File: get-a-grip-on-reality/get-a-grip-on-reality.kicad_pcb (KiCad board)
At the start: 2 copper layers, 74 parts, among them J1 HALL1, J10 MOTOR4, J11 MOTOR5, J12 Conn_01x04_Pin, J13 Conn_01x05_Pin, J14 Battery Connector Bat, J15 Battery Connector MCU, J2 HALL2, J3 HALL3, J4 HALL4, J5 HALL5, J6 Conn_01x04_Pin, J7 MOTOR1, J8 MOTOR2, J9 MOTOR3, P1 USB_C_Plug_USB2.0, U1 TLV76733DRVx, U2 ESP32-S3-WROOM-1, U3 D3V3XA4B10LP, U4 IIM-42652, U5 BQ25887, U6 TPS54KB20RZRR

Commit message: finish top pcb
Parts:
- removed the J12 at (47.1, 44.5)
- added C12: 5p, Capacitor_SMD:C_0805_2012Metric, F.Cu at (81.0, 54.6)
- added C13: 10n, Capacitor_SMD:C_0805_2012Metric, F.Cu at (73.2, 52.8)
- added D4: BPV22NF, BPV22NF:XDCR_BPV22NF, F.Cu at (80.3, 49.0)
- added D5: BPV22NF, BPV22NF:XDCR_BPV22NF, F.Cu at (86.1, 52.4)
- added D6: BPV22NF, BPV22NF:XDCR_BPV22NF, F.Cu at (86.1, 45.7)
- added J13: Conn_01x05_Pin, Connector_PinHeader_2.54mm:PinHeader_1x05_P2.54mm_Vertical, F.Cu at (46.9, 45.0)
- added R12: 5.23k, Resistor_SMD:R_0805_2012Metric, F.Cu at (47.9, 150.0)
- added R13: 30.1k, Resistor_SMD:R_0805_2012Metric, F.Cu at (45.9, 150.0)
- added R4: 3k, Resistor_SMD:R_0805_2012Metric, F.Cu at (68.6, 45.3)
- added R5: 47k, Resistor_SMD:R_0805_2012Metric, F.Cu at (68.6, 48.8)
- added R6: 100k, Resistor_SMD:R_0805_2012Metric, F.Cu at (80.9, 52.6)
- added R7: 47k, Resistor_SMD:R_0805_2012Metric, F.Cu at (72.6, 44.4)
- added TH1: 10k, Resistor_SMD:R_0805_2012Metric, F.Cu at (44.0, 150.0)
- added U5: TLV2462CDR, fydp:SOIC127P599X175-8N, F.Cu at (73.3, 49.0)
- P1, U3: moved to B.Cu
- moved P1 34.1 mm to (62.2, 75.4), turned to 180 degrees
- moved C11 28.7 mm to (58.0, 43.8)
- moved U3 23.6 mm to (63.0, 69.3), turned to -90 degrees
- moved D3 11.7 mm to (78.2, 58.1), turned to -90 degrees
- moved R2 7.35 mm to (66.5, 48.8), turned to 90 degrees
- moved R3 6.86 mm to (78.3, 54.6), turned to 90 degrees
- moved C1 4.16 mm to (73.2, 63.5)
- moved J12 4.15 mm to (76.6, 66.8)
- moved C3 3.33 mm to (72.6, 42.2)
- moved C2 3.33 mm to (79.5, 42.2)
- moved R1 3.33 mm to (76.0, 42.2)
- moved U1 3.17 mm to (73.3, 61.1)
- moved D2 2.44 mm to (66.5, 52.4), turned to -90 degrees
- moved C4 1.96 mm to (72.9, 57.8)
- moved C5 1.96 mm to (72.9, 55.7)
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- renumbered C12 to C14, C13 to C15, C14 to C16, C15 to C17, C16 to C18, C17 to C19, C18 to C20, C19 to C21, C20 to C22, C21 to C23, C22 to C24, C23 to C25, C24 to C26, C25 to C27, C26 to C28, C27 to C29, C28 to C30, D4 to D7, D5 to D8, J6 to J1, J15 to J12, J13 to J14, J14 to J15, J1 to J2, J2 to J3, J3 to J4, J4 to J5, J5 to J6, R6 to R10, R7 to R11, R8 to R14, R9 to R15, R10 to R16, R11 to R17, R12 to R18, R13 to R19, R14 to R20, R4 to R8, R5 to R9, U5 to U6, U6 to U7
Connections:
- P1 pad A4: VBUS -> +5V
- P1 pad A9: VBUS -> +5V
- P1 pad B4: VBUS -> +5V
- P1 pad B9: VBUS -> +5V
- U2 pad 16: unconnected-(U2-GPIO46_HALL4B-Pad16) -> Net-(J13-Pin_4)
- U2 pad 22: unconnected-(U2-GPIO14/TOUCH14/ADC2_CH3/FSPIWP/FSPIDQS/SUBSPIWP-Pad22) -> /Light Sensor/2OUT
- U3 pad 4: VBUS -> +5V
- U3 pad 7: VBUS -> +5V
- U6 pad 7: unconnected-(U5-TS-Pad7) -> Net-(U6-TS)
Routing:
- net +3.3V: track 0.00 -> 118.9 mm, vias 0 -> 2
- net Net-(U2-EN): track 0.00 -> 99.8 mm, vias 0 -> 2
- net +5V: track 0.00 -> 24.5 mm, vias 0 -> 3
- net /Light Sensor/1IN-: track 0.00 -> 22.3 mm
- net /MCU/USB_N: track 25.4 -> 7.63 mm, vias 0 -> 1
- net Net-(J13-Pin_3): track 0.00 -> 16.8 mm, vias 0 -> 1
- net /MCU/USB_P: track 22.8 -> 6.54 mm, vias 0 -> 1
- net /Light Sensor/2OUT: track 0.00 -> 12.8 mm
- net Net-(J13-Pin_2): track 0.00 -> 11.5 mm, vias 0 -> 1
- net /HALL4C: track 0.00 -> 10.8 mm
- net /Light Sensor/2IN+: track 0.00 -> 9.88 mm
- net /HALL4B: track 0.00 -> 9.45 mm
- net Net-(U5-1OUT): track 0.00 -> 9.36 mm
- net /HALL4A: track 0.00 -> 7.52 mm
- net /HALL5C: track 0.00 -> 4.41 mm
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- added copper zone on B.Cu, net +5V
- added copper zone on B.Cu, net GND
- added copper zone on F.Cu, net GND
- removed copper zone on F.Cu, net +BATT
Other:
- board text added: "I2C"
- board text added: "M1"
- board text added: "M2"
- board text added: "M3"
- board text added: "M4"
- board text added: "M5"

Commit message: added review comments
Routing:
- net +3.3V: track 118.9 -> 117.3 mm
- net /MCU/USB_N: track 7.63 -> 6.35 mm
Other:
- board text added: "<- Fix long 3.3v line with thin width"
- board text added: "<- GND not connected"
- board text added: "<- More vias here to reduce GND return path impedence"
- board text added: "<- Try not to put vias on pads"
- board text added: "<- add vias here"
- board text added: "Cap here ->"
- board text added: "Missing connection ->"
- board text added: "Move caps ["
- board text added: "Really thin GND path ->"
- board text added: "Rotate cap to reduce return loop V"
- board text added: "^ Right Angle grrr"

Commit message: add pdb
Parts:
- C14, C15, C16, C17, C18, C19, C20, C21, C22, C23, C24, C25, C26, C27, C28, C29, C30, D7, J14, L1, L2, R10, R11, R12, R13, R14, R15, R16, R17, R18, R19, R20, R8, R9, TH1, U6, U7: moved to B.Cu
- moved J14 54.1 mm to (88.7, 117.8), turned to 180 degrees
- moved C14 50.0 mm to (85.6, 107.8)
- moved R9 48.7 mm to (85.8, 125.1)
- moved D7 48.4 mm to (85.6, 111.5)
- moved R8 48.4 mm to (85.6, 114.9)
- moved TH1 45.2 mm to (83.8, 128.6)
- moved R17 45.2 mm to (83.8, 125.1)
- moved R13 41.7 mm to (81.8, 128.6)
- moved R18 41.7 mm to (81.8, 125.1)
- moved U6 41.2 mm to (81.5, 119.5), turned to 180 degrees
- moved L1 40.0 mm to (80.8, 113.4), turned to 180 degrees
- moved C21 39.4 mm to (80.4, 115.7), turned to 0 degrees
- moved R12 38.4 mm to (79.8, 128.6)
- moved C24 38.3 mm to (79.8, 125.1)
- moved C15 35.1 mm to (77.8, 123.5)
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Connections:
- C14 pad 1: VBUS -> +5V
- J15 pad 1: +5V -> GND
- J15 pad 2: GND -> +5V
- U6 pad 23: VBUS -> +5V
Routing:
- net /Power/CELL_1: track 0.00 -> 65.5 mm, vias 0 -> 30
- net +5V: track 24.5 -> 80.5 mm, vias 3 -> 5
- net Net-(U6-TS): track 2.74 -> 14.0 mm, vias 0 -> 2
- net Net-(U7-VCC): track 0.00 -> 10.4 mm, vias 0 -> 1
- net Net-(U7-MSEL): track 2.52 -> 6.11 mm
- net GND: track 4.32 -> 7.28 mm
- net +BATT: vias 0 -> 37
- added copper zone on B.Cu, net +BATT
- added copper zone on F.Cu, net +BATT
- added copper zone on B.Cu, net /Power/BOOT
- added copper zone on B.Cu, net /Power/CELL_1
- added copper zone on F.Cu, net /Power/CELL_1
- added copper zone on B.Cu, net /Power/PMID
- added copper zone on B.Cu, net /Power/SNS
- added copper zone on B.Cu, net /Power/SW_5
- added copper zone on B.Cu, net /Power/SW_BAT
- removed copper zone on F.Cu, net /Power/BOOT
- removed copper zone on F.Cu, net /Power/PMID
- removed copper zone on F.Cu, net /Power/SNS
- removed copper zone on F.Cu, net /Power/SW_5
- removed copper zone on F.Cu, net /Power/SW_BAT
- removed copper zone on F.Cu, net VBUS

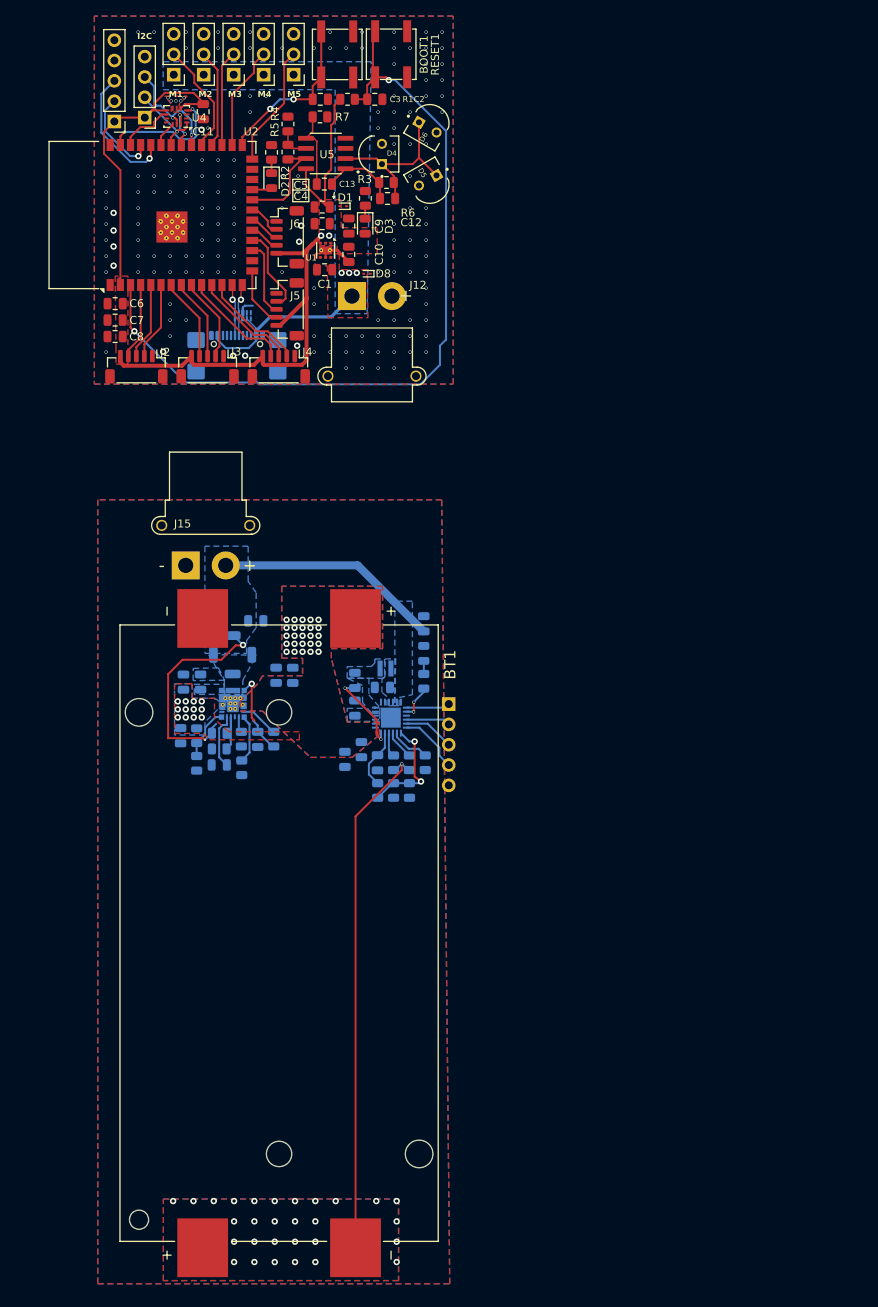
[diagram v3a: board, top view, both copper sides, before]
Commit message: finish pcb no drc errors
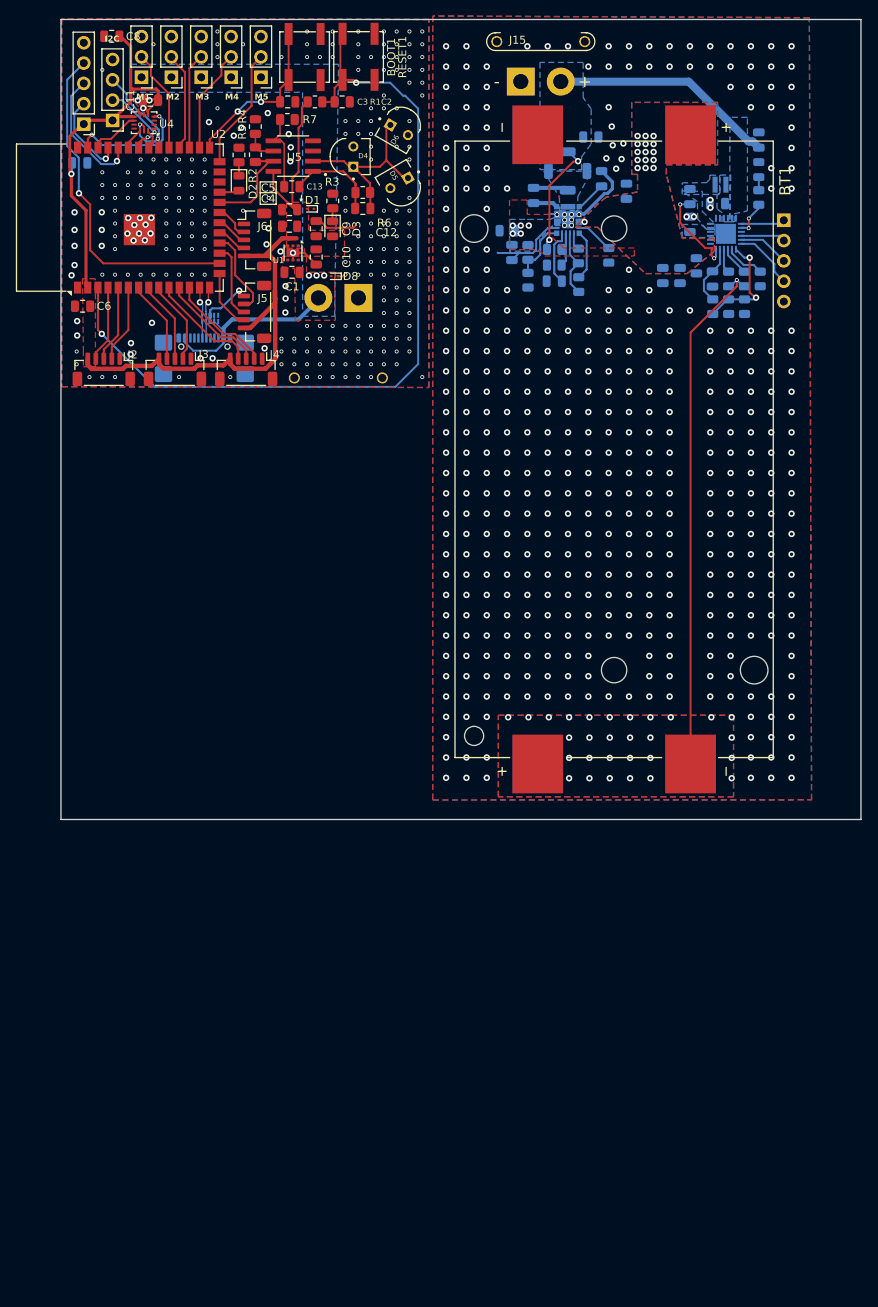
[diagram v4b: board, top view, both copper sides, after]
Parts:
- C7, J12: moved to B.Cu
- U7: footprint fydp library:RZR0016A-MFG -> fydp:RZR0016A-MFG
- moved C22 82.2 mm to (107.8, 52.1), turned to 90 degrees
- moved C20 74.7 mm to (110.9, 53.7)
- moved C27 73.7 mm to (99.3, 54.2)
- moved R15 73.6 mm to (104.9, 61.8)
- moved R16 73.6 mm to (105.0, 65.4)
- moved U7 73.6 mm to (103.6, 57.3)
- moved BT1 73.6 mm to (109.4, 86.0)
- moved C14 73.6 mm to (127.5, 47.3)
- moved C16 73.6 mm to (117.6, 64.2)
- moved C23 73.6 mm to (101.9, 64.9)
- moved C26 73.6 mm to (118.8, 57.8)
- moved D7 73.6 mm to (127.5, 51.0)
- moved J14 73.6 mm to (130.6, 57.3)
- moved R14 73.6 mm to (108.7, 61.7)
- moved R8 73.6 mm to (127.5, 54.5)
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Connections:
- J12 pad 1: +5V -> GND
- J12 pad 2: GND -> +5V
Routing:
- net GND: track 7.28 -> 50.6 mm, vias 166 -> 705
- net Net-(J13-Pin_4): track 0.00 -> 42.3 mm, vias 0 -> 1
- net +5V: track 80.5 -> 67.9 mm
- net +3.3V: track 117.3 -> 127.8 mm, vias 2 -> 1
- net Net-(U7-VCC): track 10.4 -> 4.55 mm, vias 1 -> 0
- net /Power/SW_5: track 0.00 -> 4.38 mm
- net Net-(U2-EN): track 99.8 -> 103.0 mm
- net /IMU/SDI: track 5.67 -> 2.54 mm, vias 2 -> 0
- net /Power/BOOT: track 0.00 -> 3.06 mm
- net Net-(U5-1OUT): track 9.36 -> 11.5 mm
- net /MOTOR1: track 14.1 -> 12.8 mm
- net Net-(U6-BTST): track 10.4 -> 11.6 mm
- net /Light Sensor/1IN-: track 22.3 -> 23.4 mm
- net /IMU/SDO: track 10.0 -> 11.1 mm, vias 1 -> 2
- net Net-(U7-EN): track 6.60 -> 7.60 mm
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- removed copper zone on B.Cu, net /Power/BOOT
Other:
- board outline added: 100 x 100 mm
- board text added: "Antenna"
- board text removed: "<- Fix long 3.3v line with thin width"
- board text removed: "<- GND not connected"
- board text removed: "<- More vias here to reduce GND return path impedence"
- board text removed: "<- Try not to put vias on pads"
- board text removed: "<- add vias here"
- board text removed: "Cap here ->"
- board text removed: "Missing connection ->"
- board text removed: "Move caps ["
- board text removed: "Really thin GND path ->"
- board text removed: "Rotate cap to reduce return loop V"
- board text removed: "^ Right Angle grrr"
